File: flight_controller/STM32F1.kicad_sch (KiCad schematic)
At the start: 18 parts, among them J4 SM10B-SRSS-TB (LF)(SN), U14 ESD7104MUTAG_C2987068, U15 ESD7104MUTAG_C2987068, U2 STM32F103C8T6, X1 TAXM8M4RDBCCT2T

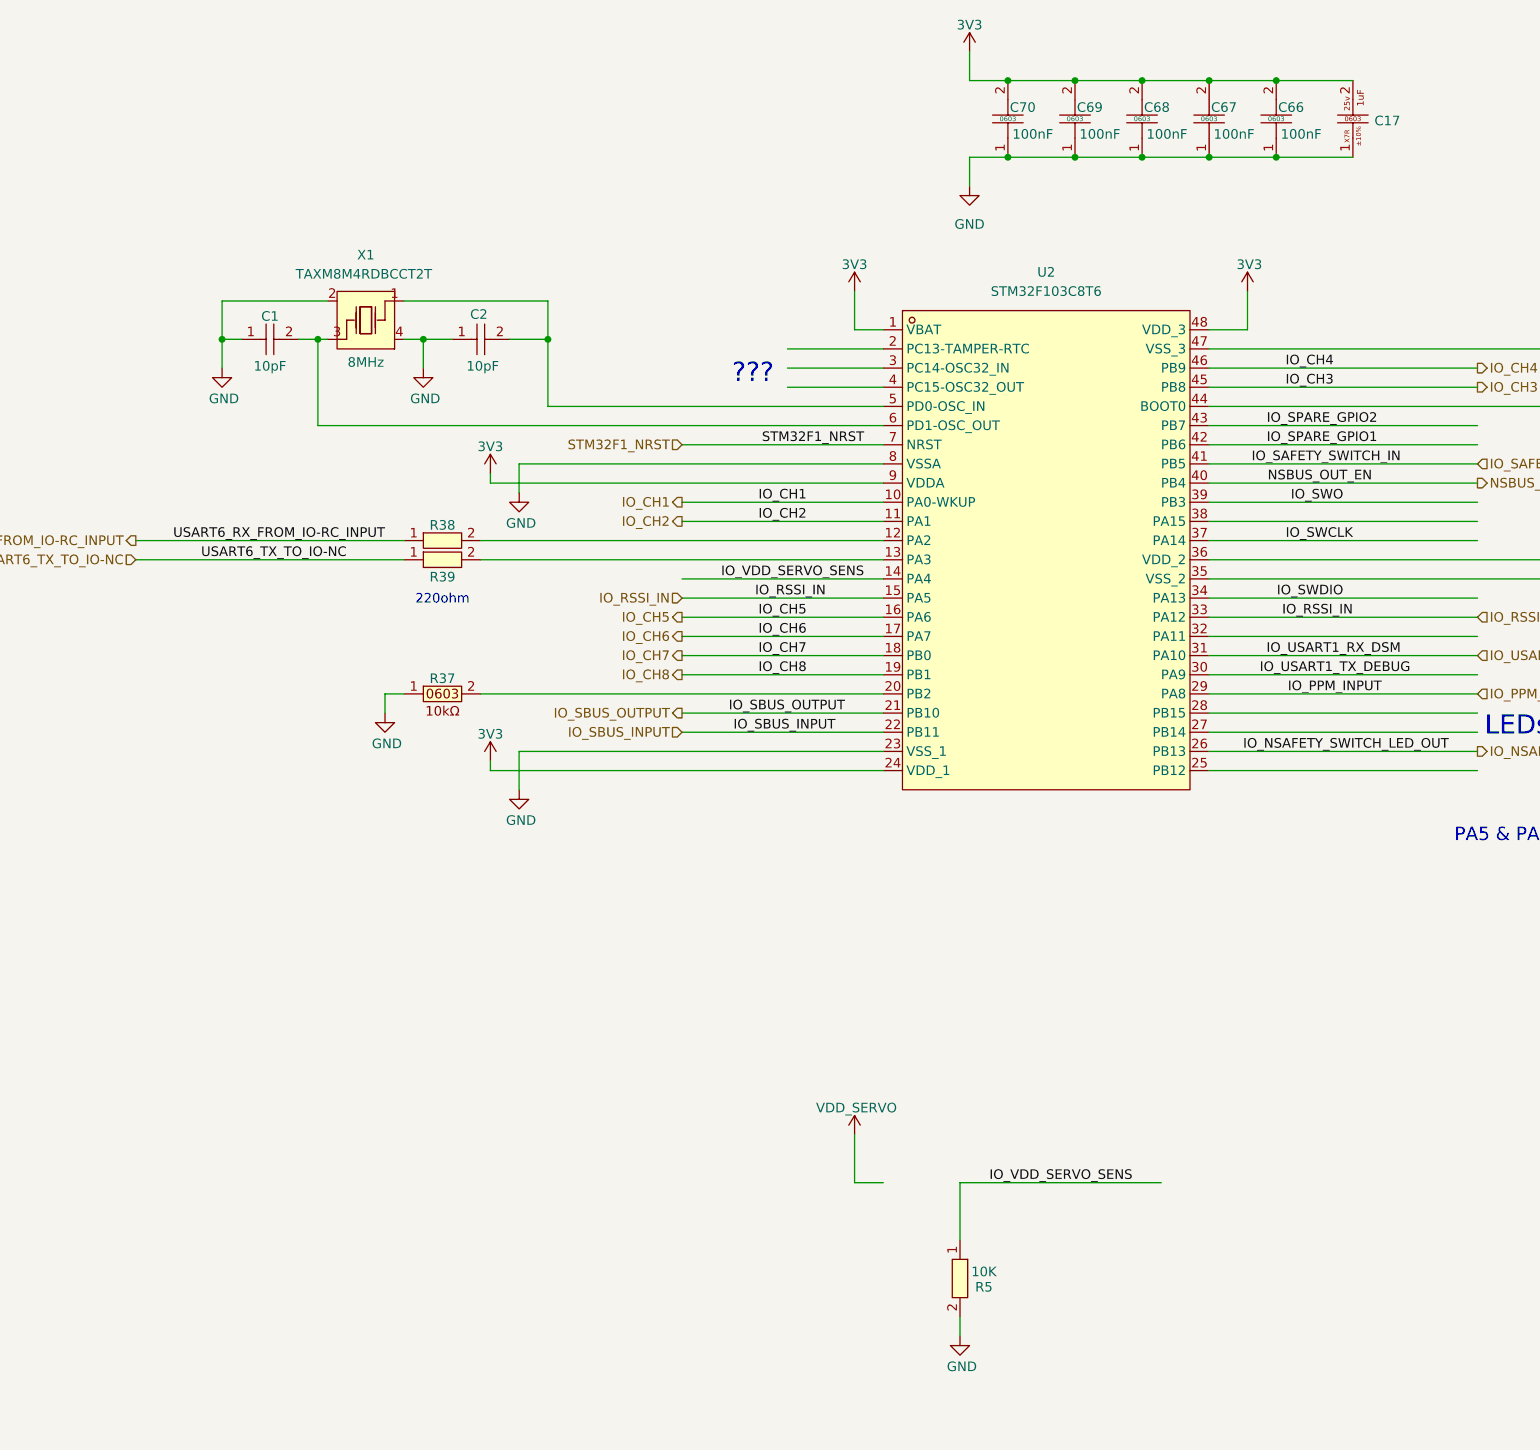
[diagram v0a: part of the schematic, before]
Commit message: updating symbols as in the shared library
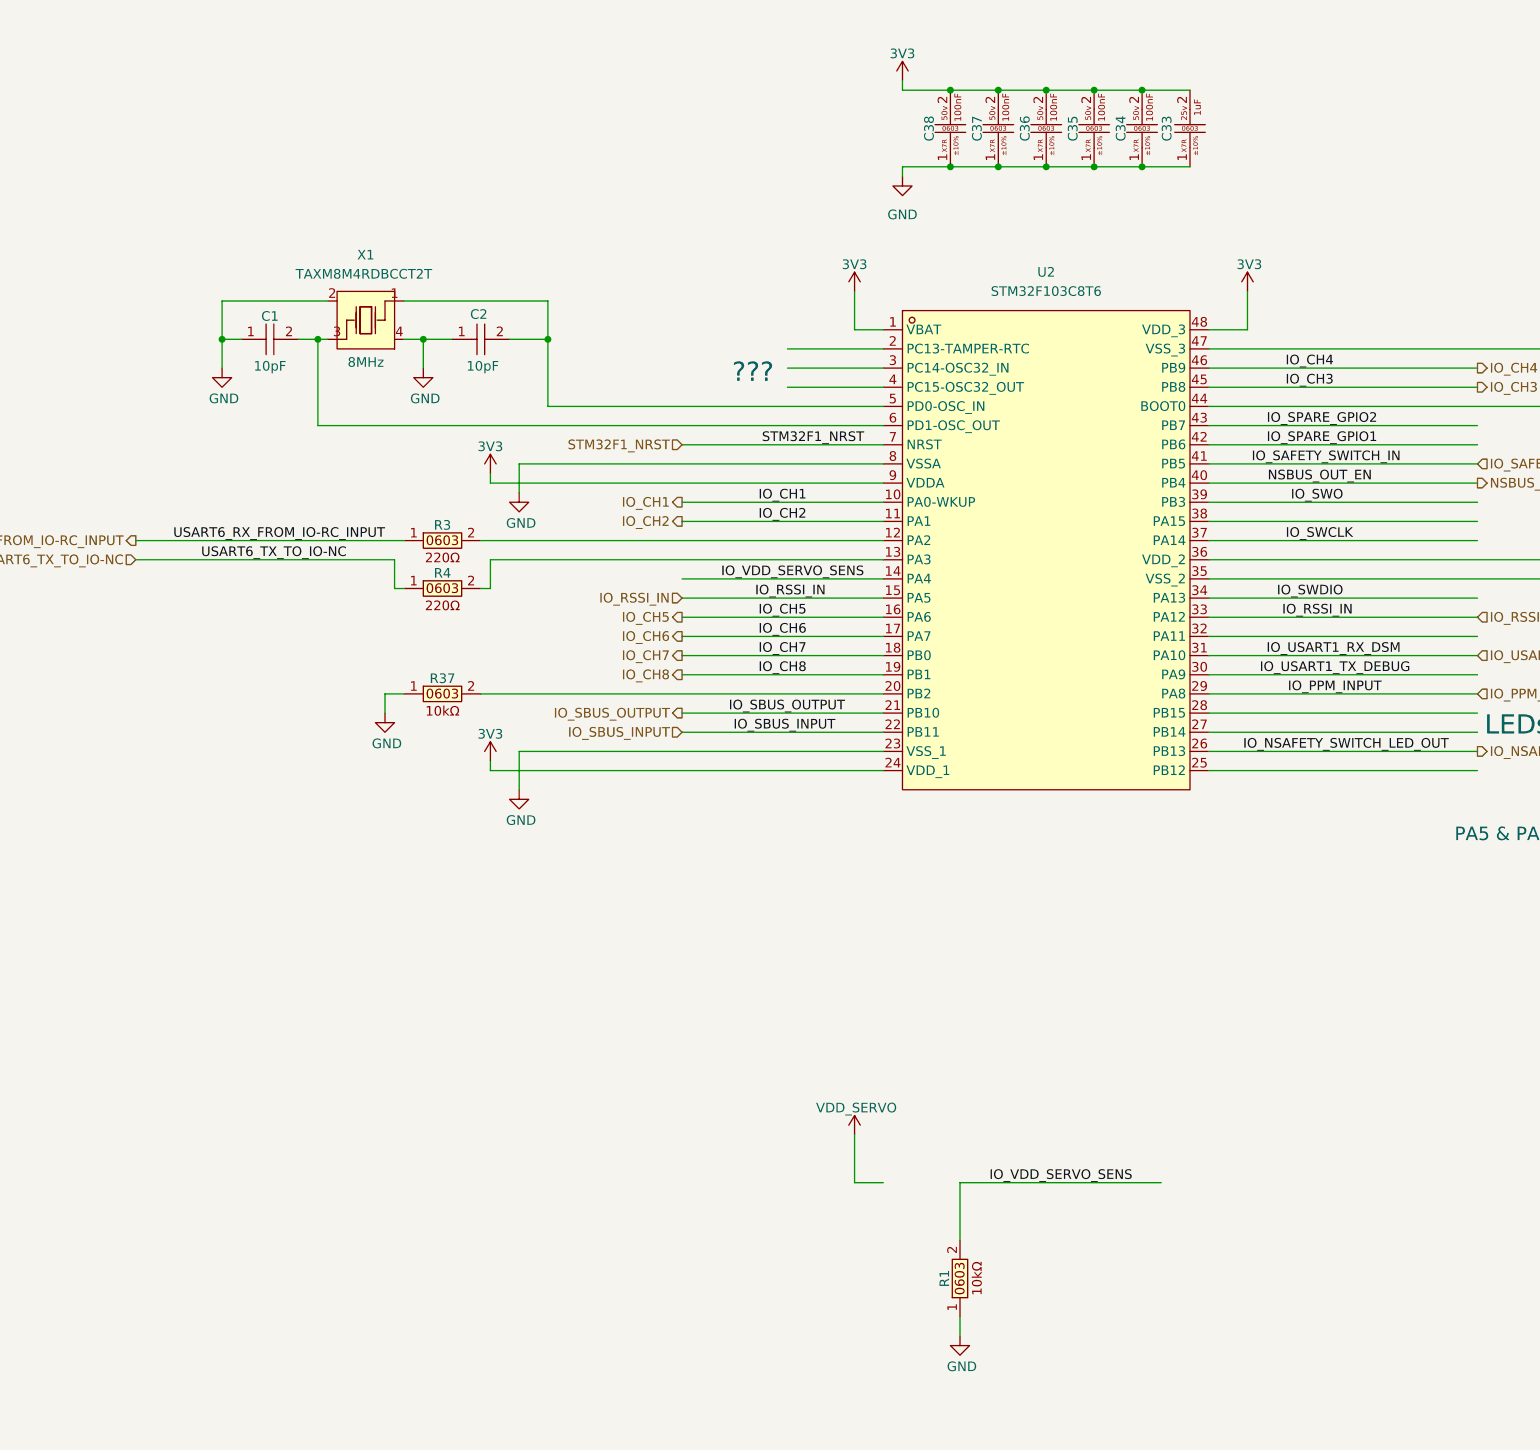
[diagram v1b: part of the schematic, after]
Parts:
- removed C17: CL10B105KA8NNNC (1uf ,0603 ,25v ,X7R), easyeda2kicad:C0603, symbol lampelKicadLIB:CL10B105KA8NNNC (1uf ,0603 ,25v ,X7R)
- removed C66, C67, C68, C69, C70: CC0603KRX7R9BB104, easyeda2kicad:C0603, symbol easyeda2kicad:CC0603KRX7R9BB104
- removed R38, R39: 0603WAF2200T5E, easyeda2kicad:R0603, symbol lampelKicadLIB:0603WAF2200T5E
- removed R5: 0402WGF1002TCE, easyeda2kicad:R0402, symbol easyeda2kicad:0402WGF1002TCE
- added C33: CL10B105KA8NNNC (1uf ,0603 ,25v ,X7R), easyeda2kicad:C0603, symbol lampelKicadLIB:CL10B105KA8NNNC (1uf ,0603 ,25v ,X7R)
- added C34, C35, C36, C37, C38: CC0603KRX7R9BB104 (100nf , 0603 ,50v ,X7R), easyeda2kicad:C0603, symbol lampelKicadLIB:CC0603KRX7R9BB104 (100nf , 0603 ,50v ,X7R)
- added R1: 603WAF1002T5E (10kohm , 0603), easyeda2kicad:R0603, symbol lampelKicadLIB:0603WAF1002T5E (10kohm , 0603)
- added R3, R4: 0603WAF2200T5E (220ohm , 0603), easyeda2kicad:R0603, symbol lampelKicadLIB:0603WAF2200T5E (220ohm , 0603)
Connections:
- net 3V3: now also C33.2, C34.2, C35.2, C36.2, C37.2, C38.2
- net GND: now also C33.1, C34.1, C35.1, C36.1, C37.1, C38.1, R1.1
- net IO_VDD_SERVO_SENS: now also R1.2
- net USART6_RX_FROM_IO-RC_INPUT: now also R3.1
- net USART6_TX_TO_IO-NC: now also R4.1
- net at U2.12 (PA2): now also R3.2
- net at U2.13 (PA3): now also R4.2
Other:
- note removed: "220ohm"

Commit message: update debug conn
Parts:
- removed J4: SM10B-SRSS-TB (LF)(SN), easyeda2kicad:CONN-SMD_10P-P1.00_SM10B-SRSS-TB-LF-SN, symbol easyeda2kicad:SM10B-SRSS-TB(LF)(SN)
- removed U14, U15: ESD7104MUTAG_C2987068, easyeda2kicad:DFN-10_L2.5-W1.0-P0.50-BL, symbol easyeda2kicad:ESD7104MUTAG_C2987068
- removed X1: TAXM8M4RDBCCT2T, easyeda2kicad:CRYSTAL-SMD_4P-L3.2-W2.5-BL, symbol easyeda2kicad:TAXM8M4RDBCCT2T
- added D11: KT-0603R, easyeda2kicad:LED0603-RD, symbol easyeda2kicad:KT-0603R
- added D4: 0603 Green 509-620mcd, easyeda2kicad:LED0603-RD, symbol easyeda2kicad:0603Green509-620mcd
- added R51, R52, R53: 603WAF1000T5E (100ohm , 0603), easyeda2kicad:R0603, symbol lampelKicadLIB:0603WAF1000T5E (100ohm , 0603)
- added SW3: 6.0*6.0*6.0, easyeda2kicad:SW-SMD_4P-L6.0-W6.0-P4.50-LS8.6, symbol easyeda2kicad:6.0*6.0*6.0
- added U12: HB-PH9-12727PB2GOB, easyeda2kicad:HDR-SMD_14P-P1.27-V-M-R2-C7-LS5.5, symbol easyeda2kicad:HB-PH9-12727PB2GOB
- added X3: TAXM8M4RDBCCT2T, easyeda2kicad:CRYSTAL-SMD_4P-L3.2-W2.5-BL, symbol lampelKicadLIB:TAXM8M4RDBCCT2T
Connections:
- net 3V3: now also U12.3
- net GND: now also D11.1 (K), D4.1 (K), R51.2, SW3.3, SW3.4, U12.5, U12.7, X3.2, X3.4
- net IO_SWCLK: now also U12.6
- net IO_SWDIO: now also U12.4
- net IO_SWO: now also U12.8
- net STM32F1_NRST: now also SW3.1, SW3.2
- net at C2.2, U2.5 (PD0-OSC_IN): now also X3.1
- net at C1.2, U2.6 (PD1-OSC_OUT): now also X3.3
- new net: R51.1, U12.11
- new net: D11.2 (A), R53.1
- new net: D4.2 (A), R52.1
- new net LED1: R52.2
- new net LED2: R53.2
- new net UART2_VCP_RX: U12.13
- new net UART2_VCP_TX: U12.14
- no-connect marks 0 -> 5
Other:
- note added: "JTAG/SW CONN"
- note added: "LEDS"
- note added: "NRST has an internal pullup"
- note added: "Original part number for the stm32 v3 set is : FTSH-107-01-L-DV-K-A"
- note added: "update"
- moved on the sheet: R1

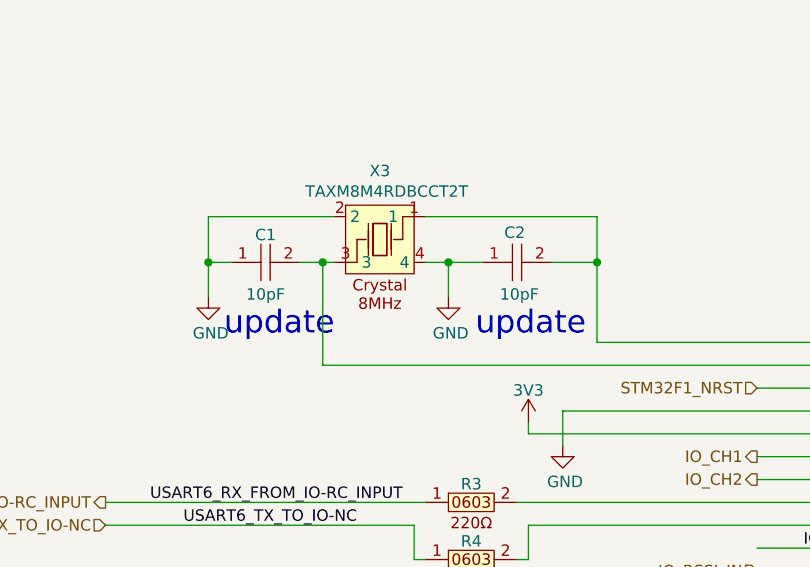
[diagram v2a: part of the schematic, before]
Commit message: gps and power blocks
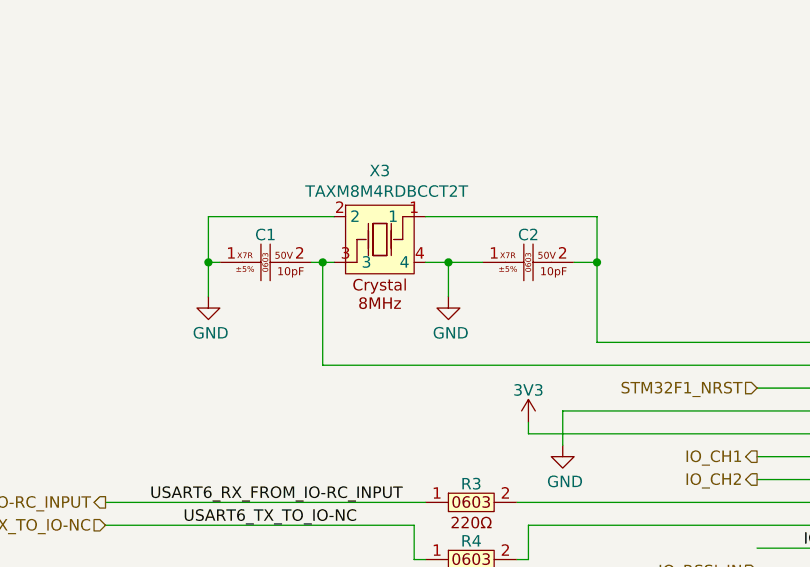
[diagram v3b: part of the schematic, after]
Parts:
- removed C1, C2: CC0603JRNPO9BN100, easyeda2kicad:C0603, symbol easyeda2kicad:CC0603JRNPO9BN100
- added C1, C2: CC0603JRNPO9BN100 (10pF , 0603 ,50V ,X7R), easyeda2kicad:C0603, symbol lampelKicadLIB:CC0603JRNPO9BN100 (10pF , 0603 ,50V ,X7R)
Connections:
- net GND: now also C1.1, C2.1
- net at U2.5 (PD0-OSC_IN), X3.1: now also C2.2
- net at U2.6 (PD1-OSC_OUT), X3.3: now also C1.2
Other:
- note removed: "update"

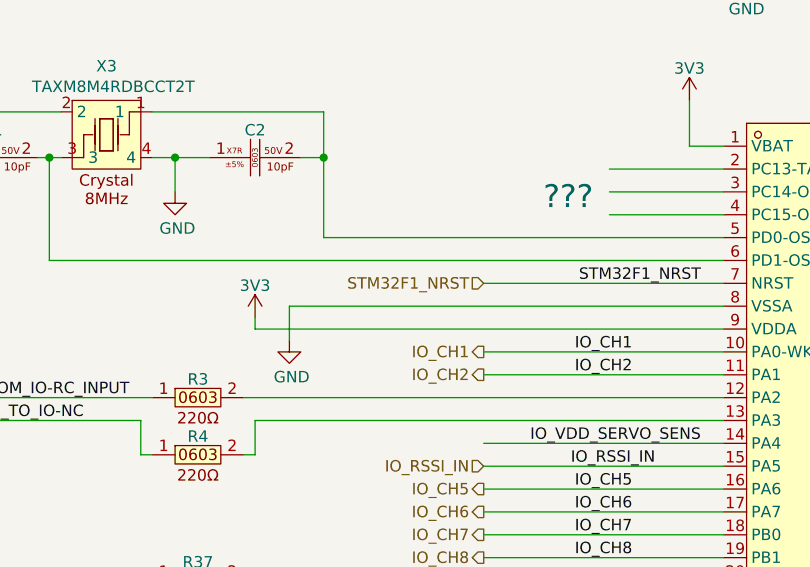
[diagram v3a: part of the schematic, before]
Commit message: ALL CONNECTORS, ETH, SERVO,RC,SPI,FLASH and more. to finish GPSand STM32 PINOUT
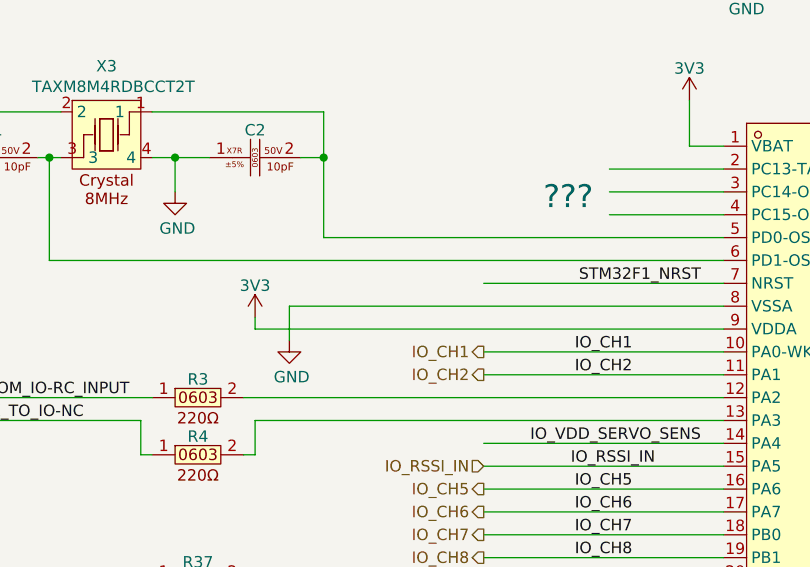
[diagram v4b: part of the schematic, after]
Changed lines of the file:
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@@
-		)
-	)
-	(hierarchical_label "STM32F1_NRST"
-		(shape input)
-		(at 306.07 137.16 180)
-		(effects
-			(font
-				(size 1.27 1.27)
-			)
-			(justify right)
 		)
 	)

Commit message: cleanup and improvements
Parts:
- removed R1: 603WAF1002T5E (10kohm , 0603), easyeda2kicad:R0603, symbol lampelKicadLIB:0603WAF1002T5E (10kohm , 0603)
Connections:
- net LED1 is gone; now on net IO_LED1: R52.2
- net LED2 is gone; now on net IO_LED2: R53.2
- net UART2_VCP_RX is gone; now on net IO_USART1_RX_DSM_VCP: U12.13
- net UART2_VCP_TX is gone; now on net IO_USART1_TX_VCP: U12.14
- net 3V3: now also D11.2 (A), D4.2 (A)
- net GND: no longer D11.1 (K), D4.1 (K)
- net FMU_USART6_RX_IO_USART2_TX: now reaches R3.2, U2.12 (PA2)
- net FMU_USART6_TX_IO_USART2_RX: now reaches R4.2, U2.13 (PA3)
- net IO_LED2: now reaches U2.27 (PB14)
- net IO_LED1: now reaches U2.28 (PB15)
- net at R53.1: now also D11.1 (K); no longer D11.2 (A)
- net at R52.1: now also D4.1 (K); no longer D4.2 (A)
- net IO_USART1_RX_DSM renamed IO_USART1_RX_DSM_VCP
- net IO_USART1_TX_DEBUG renamed IO_USART1_TX_VCP
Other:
- note added: "* PA5 & PA12 SAME NAME"
- note removed: "???"
- note removed: "LEDs??"
- note removed: "PA5 & PA12 SAME NAME??"
- moved on the sheet: D11, D4, R3, R4, R52, R53
